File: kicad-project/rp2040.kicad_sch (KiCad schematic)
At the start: 31 parts

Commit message: hw: update to complete schematic
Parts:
- removed J?: Conn_02x08_Counter_Clockwise, Connector_PinHeader_2.54mm:PinHeader_2x05_P2.54mm_Vertical, symbol Connector_Generic:Conn_02x05_Counter_Clockwise
- removed J?: Conn_02x03_Counter_Clockwise, Connector_PinHeader_2.54mm:PinHeader_2x03_P2.54mm_Vertical, symbol Connector_Generic:Conn_02x03_Counter_Clockwise
- gave numbers to parts that had none: 29
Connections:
- net GPIO1 is gone; now on net LED_G: U3.3 (GPIO1)
- net GPIO2 is gone; now on net LED_R: U3.4 (GPIO2)
- net GPIO3 is gone; now on net LED_B: U3.5 (GPIO3)
- net GPIO4 is gone; now on net ~{EN_SW}: U3.6 (GPIO4)
- net GPS_TIMEPULSE is gone; now on net ESP_RX: U3.35 (GPIO23)
- net LED_B: no longer U3.12 (GPIO9)
- net LED_G: no longer U3.9 (GPIO7)
- net LED_R: no longer U3.11 (GPIO8)
- net ~{EN_SW}: no longer U3.7 (GPIO5)
- net ACC_INT renamed LS4
- net Buzzer renamed BUZZER
- net CMP_DRDY renamed LS3
- net GPS_EN renamed ESP_TX
- net I2C1_SCL renamed LS2
- net I2C1_SDA renamed LS1
- net M1_W11 renamed ME_W11
- net M1_W12 renamed ME_W12
- net M1_W21 renamed ME_W21
- net M1_W22 renamed ME_W22
- net M2_W11 renamed STEP_C
- net M2_W12 renamed DIR_C
- net M2_W21 renamed STEP_D
- net M2_W22 renamed DIR_D
- net UART1_RX renamed I2C_SCL
- net UART1_TX renamed I2C_SDA
- net xxx renamed STEP_A
- new net DIR_A: U3.9 (GPIO7)
- new net DIR_B: U3.12 (GPIO9)
- new net EN_MOTORS: U3.7 (GPIO5)
- new net STEP_B: U3.11 (GPIO8)
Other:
- note removed: "Debug"
- note removed: "Expansion"
- moved on the sheet: C10, C11, C12, C13, C14, C15, C16, C17, C18, C19, C20, C21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

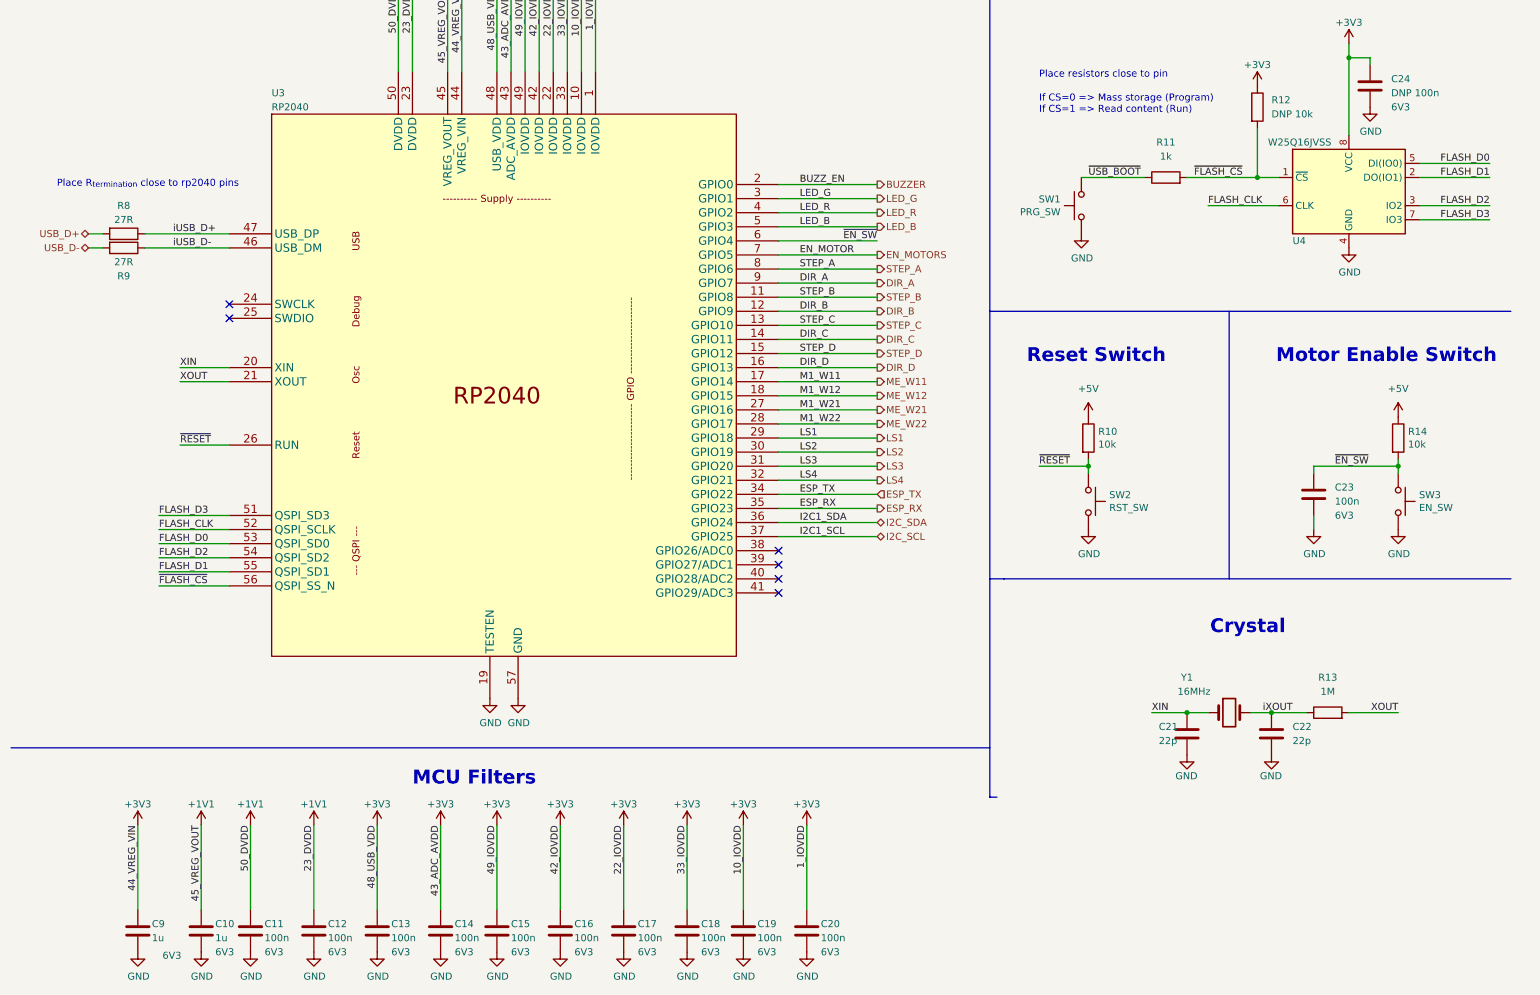
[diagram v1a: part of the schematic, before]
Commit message: hw: finish schematic, PS i2c R_pull-up wrong
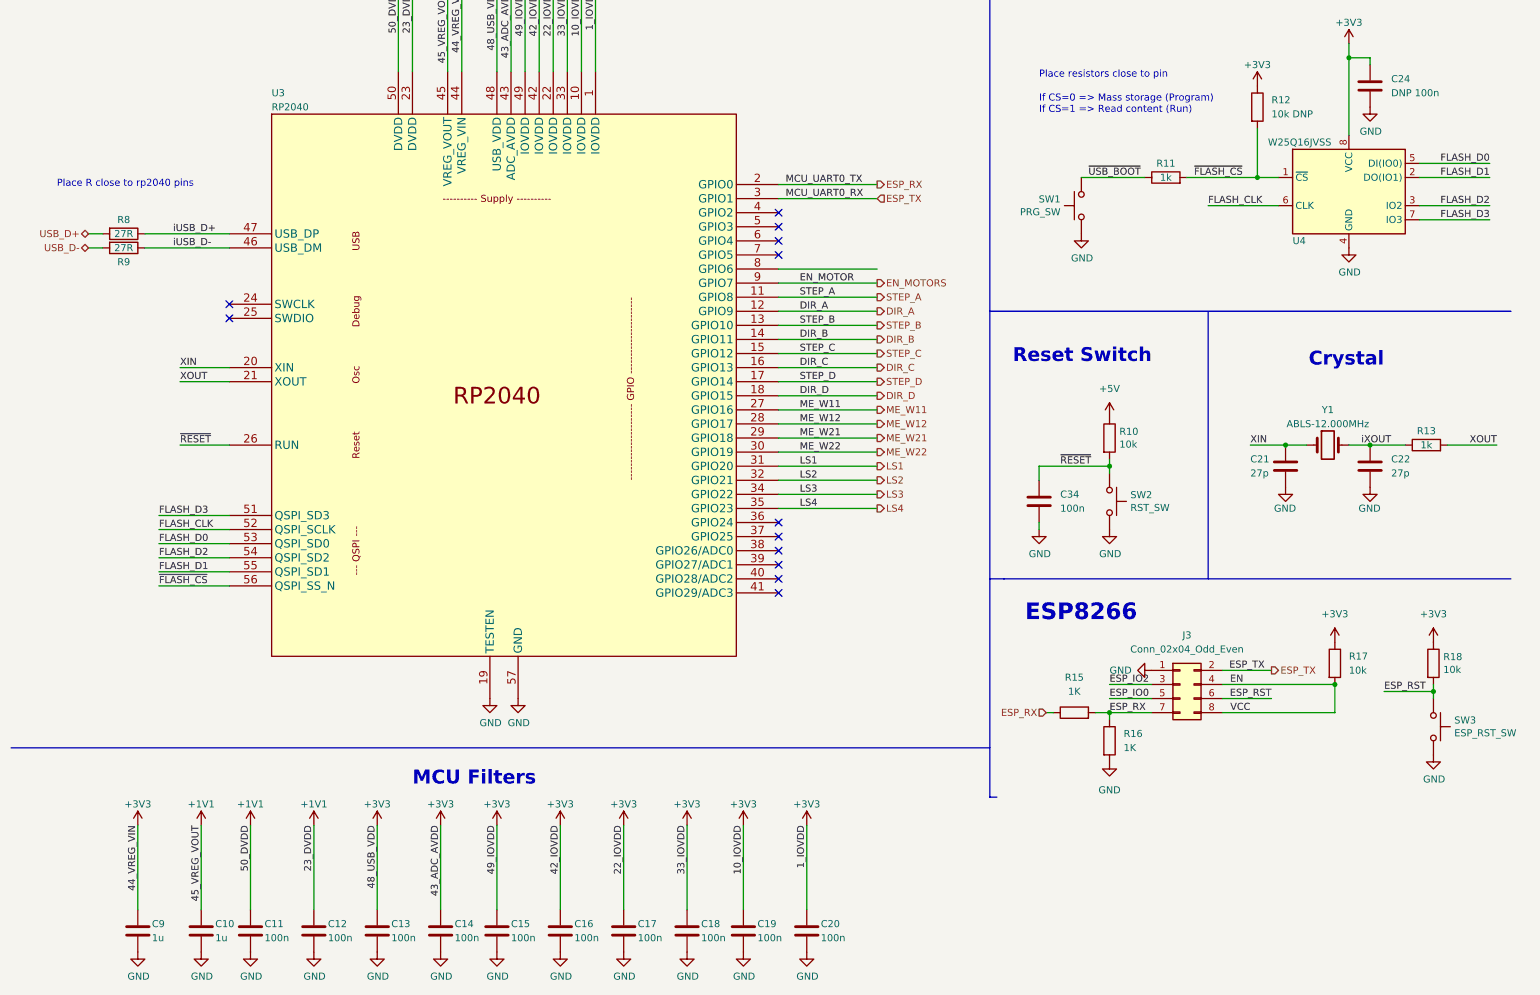
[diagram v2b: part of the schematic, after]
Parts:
- removed C23: 100n, Capacitor_SMD:C_0603_1608Metric, symbol Device:C
- removed R14: 10k, Resistor_SMD:R_0603_1608Metric, symbol Device:R
- added C34: 100n, Capacitor_SMD:C_0603_1608Metric, symbol Device:C
- added J3: Conn_02x04_Odd_Even, Connector_PinHeader_2.54mm:PinHeader_2x04_P2.54mm_Vertical, symbol Connector_Generic:Conn_02x04_Odd_Even
- added R15, R16: 1K, Resistor_SMD:R_0603_1608Metric, symbol Device:R
- added R17, R18: 10k, Resistor_SMD:R_0603_1608Metric, symbol Device:R
- C10, C11, C12, C13, C14, C15, C16, C17, C18, C19, C20, C24, C9: Voltage 6V3 -> (none)
- C21, C22: value 22p -> 27p
- R12: value DNP 10k -> 10k DNP
- R13: value 1M -> 1k
- SW1, SW2: footprint Button_Switch_THT:SW_PUSH_6mm -> Button_Switch_SMD:SW_Push_1P1T_NO_CK_KMR2
- SW3: value EN_SW -> ESP_RST_SW; footprint Button_Switch_THT:SW_PUSH_6mm -> Button_Switch_SMD:SW_Push_1P1T_NO_CK_KMR2
- Y1: value 16MHz -> ABLS-12.000MHz
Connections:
- net BUZZER is gone; now on net ESP_RX: U3.2 (GPIO0)
- net LED_G is gone; now on net ESP_TX: U3.3 (GPIO1)
- net +3V3: now also R17.1, R18.1
- net DIR_A: now also U3.12 (GPIO9); no longer U3.9 (GPIO7)
- net DIR_B: now also U3.14 (GPIO11); no longer U3.12 (GPIO9)
- net DIR_C: now also U3.16 (GPIO13); no longer U3.14 (GPIO11)
- net DIR_D: now also U3.18 (GPIO15); no longer U3.16 (GPIO13)
- net EN_MOTORS: now also U3.9 (GPIO7); no longer U3.7 (GPIO5)
- net ESP_RX: now also J3.7 (Pin_7), R15.1, R15.2, R16.1; no longer U3.35 (GPIO23)
- net ESP_TX: now also J3.2 (Pin_2); no longer U3.34 (GPIO22)
- net GND: now also C34.2, J3.1 (Pin_1), R16.2
- net LS1: now also U3.31 (GPIO20); no longer U3.29 (GPIO18)
- net LS2: now also U3.32 (GPIO21); no longer U3.30 (GPIO19)
- net LS3: now also U3.34 (GPIO22); no longer U3.31 (GPIO20)
- net LS4: now also U3.35 (GPIO23); no longer U3.32 (GPIO21)
- net ME_W11: now also U3.27 (GPIO16); no longer U3.17 (GPIO14)
- net ME_W12: now also U3.28 (GPIO17); no longer U3.18 (GPIO15)
- net ME_W21: now also U3.29 (GPIO18); no longer U3.27 (GPIO16)
- net ME_W22: now also U3.30 (GPIO19); no longer U3.28 (GPIO17)
- net STEP_A: now also U3.11 (GPIO8); no longer U3.8 (GPIO6)
- net STEP_B: now also U3.13 (GPIO10); no longer U3.11 (GPIO8)
- net STEP_C: now also U3.15 (GPIO12); no longer U3.13 (GPIO10)
- net STEP_D: now also U3.17 (GPIO14); no longer U3.15 (GPIO12)
- net ~{RESET}: now also C34.1
- net I2C_SCL: no longer names the net of U3.37 (GPIO25)
- net I2C_SDA: no longer names the net of U3.36 (GPIO24)
- net LED_B: no longer names the net of U3.5 (GPIO3)
- net LED_R: no longer names the net of U3.4 (GPIO2)
- net ~{EN_SW}: no longer names the net of U3.6 (GPIO4)
- net ~{EN_SW}: no longer SW3.1
- new net EN: J3.4 (Pin_4), J3.8 (Pin_8), R17.2
- new net ESP_IO0: J3.5 (Pin_5)
- new net ESP_IO2: J3.3 (Pin_3)
- new net ESP_RST: J3.6 (Pin_6), R18.2, SW3.1
- no-connect marks 6 -> 12
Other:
- note added: "ESP8266"
- note added: "Place R close to rp2040 pins"
- note removed: "Motor Enable Switch"
- note removed: "Place R_{termination} close to rp2040 pins"
- moved on the sheet: C21, C22, R10, R13, SW2, Y1
